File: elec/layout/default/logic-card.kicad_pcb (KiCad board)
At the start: 2 copper layers, 76 x 68 mm, 51 parts, among them U1 <help! no value>, U10 <help! no value>, U11 <help! no value>, U12 <help! no value>, U13 <help! no value>, U14 <help! no value>, U15 <help! no value>, U16 <help! no value>, U17 <help! no value>, U18 <help! no value>, U2 <help! no value>, U3 <help! no value>, U4 <help! no value>, U5 <help! no value>, U6 <help! no value>, U7 <help! no value>, U8 <help! no value>, U9 <help! no value>

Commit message: switch to coin cells
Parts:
- added U3: <help! no value>, lib:BAT-TH_BS-02-A1AJ010, B.Cu at (135.8, 120.6)
- added U4: <help! no value>, lib:BAT-TH_BS-02-A1AJ010, B.Cu at (161.3, 117.4)
- U2: footprint lib:BAT-TH_BH-AAA-A1AJ024 -> lib:BAT-TH_BS-02-A1AJ010
- moved U2 16.2 mm to (134.1, 92.8)
- renumbered U8 to U10, U9 to U11, U10 to U12, U11 to U13, U12 to U14, U13 to U15, U14 to U16, U15 to U17, U16 to U18, U17 to U19, U18 to U20, U3 to U5, U4 to U6, U5 to U7, U6 to U8, U7 to U9
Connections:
- C11 pad 1: vcc-2 -> vcc-3
- C12 pad 1: vcc-2 -> vcc-3
- C13 pad 1: vcc-2 -> vcc-3
- C14 pad 1: vcc-2 -> vcc-3
- U12 pad A4: vcc-3 -> vcc-4
- U12 pad A9: vcc-3 -> vcc-4
- U12 pad B4: vcc-3 -> vcc-4
- U12 pad B9: vcc-3 -> vcc-4
- U13 pad 2: vcc-3 -> vcc-4
- U2 pad 1: gnd -> gnd-1
- U2 pad 2: plus -> vcc-2
- U5 pad 1: plus -> vcc-2
- U7 pad 23: vcc-2 -> vcc-3
- U7 pad 45: vcc-2 -> vcc-3
- U7 pad 50: vcc-2 -> vcc-3
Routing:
- net plus: track 37.9 -> 0.00 mm
- net gnd-2: track 0.00 -> 35.1 mm
- net vcc-3: track 11.3 -> 33.3 mm, vias 0 -> 2
- net vcc-2: track 30.4 -> 44.5 mm, vias 2 -> 0
- net vcc-4: track 0.00 -> 11.3 mm
- net gnd-1: track 0.00 -> 8.49 mm
- net io3: track 14.3 -> 15.6 mm
- net gnd: vias 19 -> 21
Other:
- board text added: "San Francisco, December 2023"

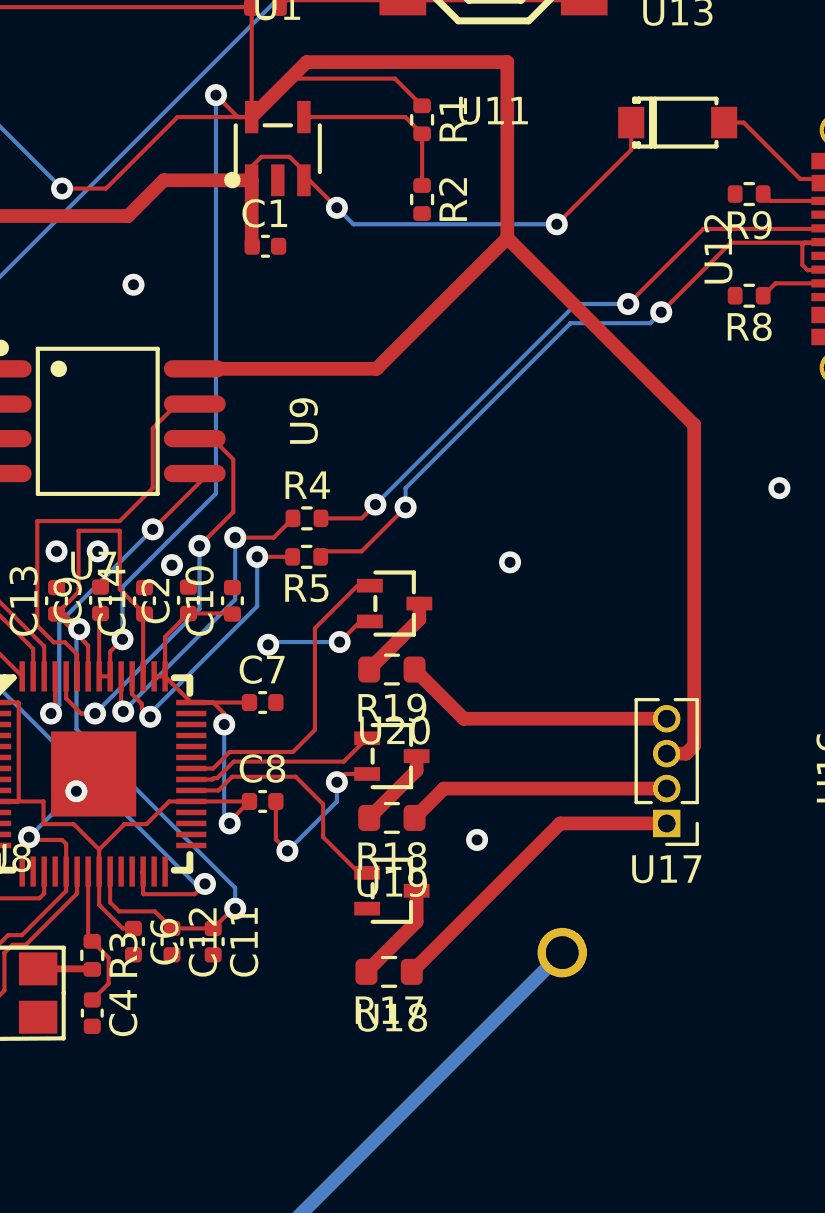
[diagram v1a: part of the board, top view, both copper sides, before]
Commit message: fix the led pins
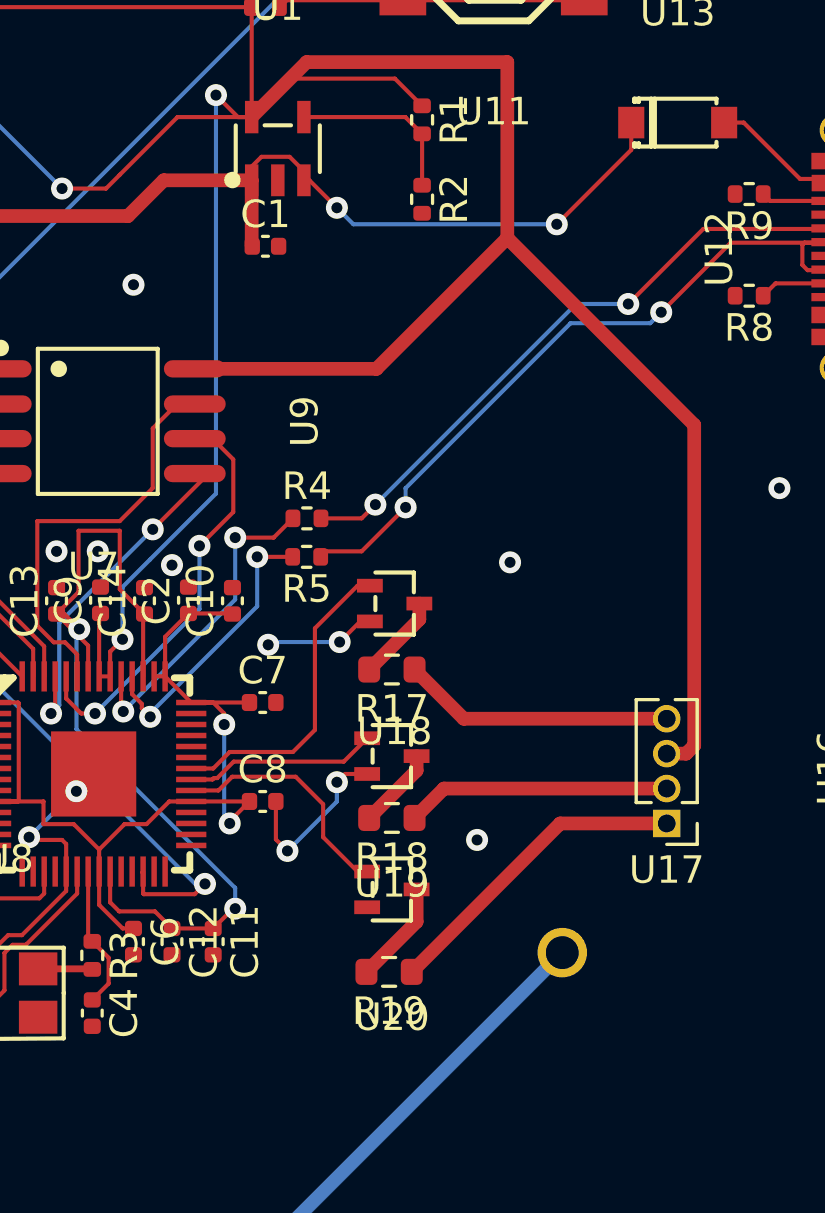
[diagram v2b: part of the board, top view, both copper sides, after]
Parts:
- C1, C10, C14, C2: value 1uF -> 1.0 uF
- C11, C12, C13, C5, C6, C7, C8, C9: value 100nF -> 100.0 nF
- C3, C4: value 20pF -> 22.0 pF
- R1: value 18k -> 18.0 KΩ
- R10, R11, R12, R13, R14, R15, R16, R2, R6, R7: value 10k -> 10.0 KΩ
- R17: value 1.5k -> 1.5 KΩ
- R18, R19: value 100 -> 100.0 Ω
- R3: value 1k -> 1.0 KΩ
- R4, R5: value 27R -> 27.0 Ω
- R8, R9: value 5.1k -> 4.7 KΩ
- U1, U10, U11, U12, U13, U14, U15, U16, U17, U18, U19, U2, U20, U3, U4, U5, U6, U7, U8, U9: value <help! no value> -> (none)
- moved R17 11.0 mm to (155.1, 97.1)
- moved R19 11.0 mm to (155.0, 108.1)
- moved U18 10.5 mm to (155.2, 94.7)
- moved U20 10.4 mm to (155.1, 105.1)
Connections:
- U17 pad 1: p1-1 -> p1-3
- U17 pad 4: p1-3 -> p1-1
- U18 pad 1: gpio22 -> gpio24
- U20 pad 1: gpio24 -> gpio22
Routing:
- net p1-3: track 9.92 -> 11.5 mm
- net p1-1: track 11.5 -> 9.92 mm
- net r_sink: track 3.71 -> 3.16 mm
- net b_sink: track 3.16 -> 3.71 mm

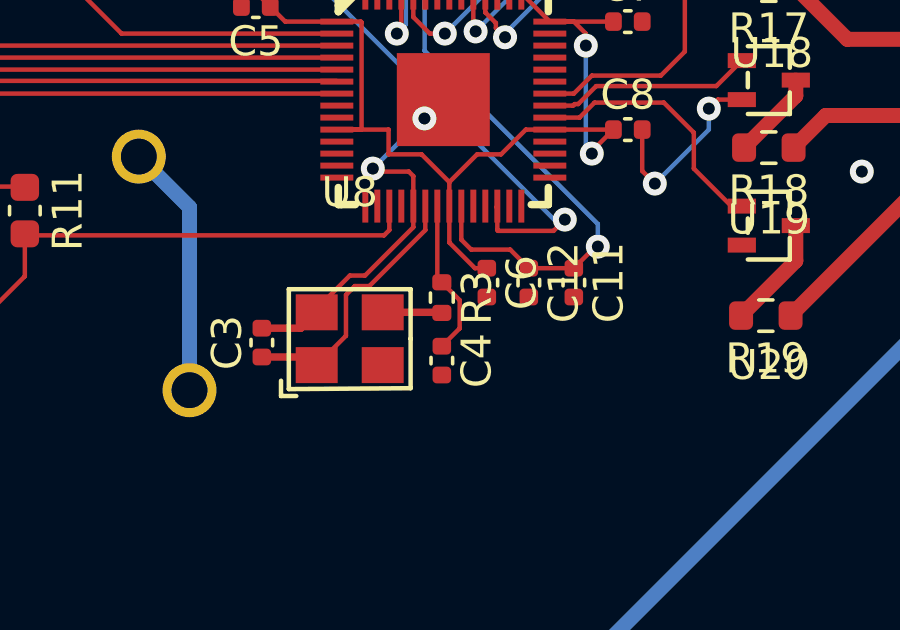
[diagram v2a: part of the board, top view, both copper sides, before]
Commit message: fix oscillator
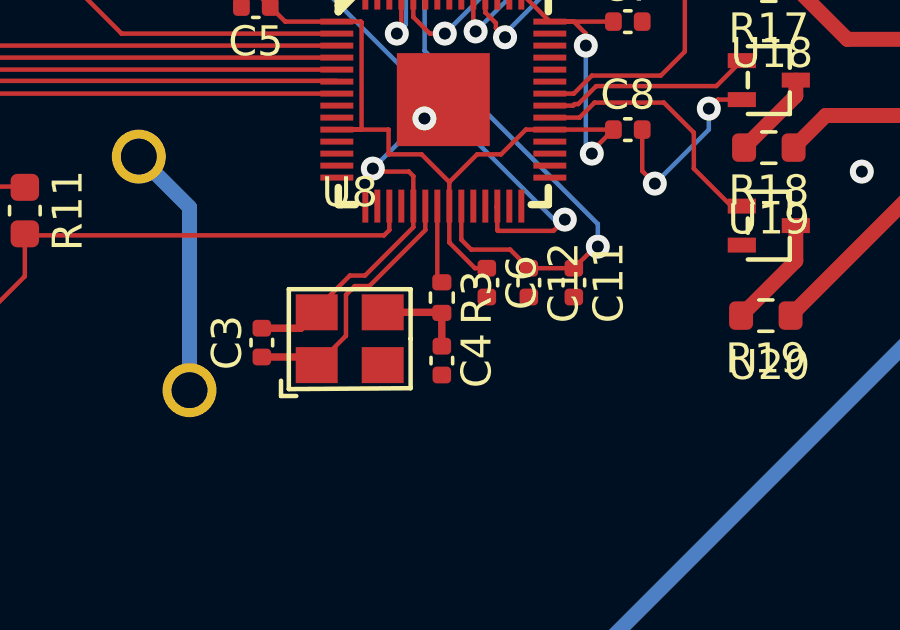
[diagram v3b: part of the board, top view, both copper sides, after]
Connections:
- C4 pad 1: p1 -> out-1
- R17 pad 1: p1-1 -> p1
- R18 pad 1: p1-2 -> p1-1
- R19 pad 1: p1-3 -> p1-2
- R3 pad 1: p1 -> xout
- U17 pad 1: p1-3 -> p1-2
- U17 pad 2: p1-2 -> p1-1
- U17 pad 4: p1-1 -> p1
- U7 pad 21: p1 -> xout
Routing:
- net p1-3: track 11.5 -> 0.00 mm
- net p1: track 5.23 -> 9.92 mm
- net xout: track 0.00 -> 2.60 mm
- net p1-2: track 9.62 -> 11.5 mm
- net out-1: track 1.98 -> 3.09 mm

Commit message: fix the build
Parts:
- C1, C10, C14, C2: value 1.0 uF -> Multilayer Ceramic Capacitors MLCC - SMD/SMT 1uF 6.3V 0402 RoHS
- C11, C12, C13, C5, C6, C7, C8, C9: value 100.0 nF -> Multilayer Ceramic Capacitors MLCC - SMD/SMT 100nF 10V 0402 RoHS
- C3, C4: value 22.0 pF -> Multilayer Ceramic Capacitors MLCC - SMD/SMT 20pF 50V 0402 RoHS
- R1: value 18.0 KΩ -> Chip Resistor - Surface Mount 18KOhms ±5% 1/16W 0402 RoHS
- R10, R11: value 10.0 KΩ -> Chip Resistor - Surface Mount 11KOhms ±5% 1/16W 0402 RoHS; footprint lib:C0603 -> lib:R0402
- R12, R13, R14, R15, R16, R2, R6, R7: value 10.0 KΩ -> Chip Resistor - Surface Mount 10KOhms ±5% 1/16W 0402 RoHS
- R17: value 1.5 KΩ -> Chip Resistor - Surface Mount 1.5KOhms ±5% 1/10W 0603 RoHS
- R18, R19: value 100.0 Ω -> Chip Resistor - Surface Mount 100Ohms ±5% 1/10W 0603 RoHS
- R3: value 1.0 KΩ -> Chip Resistor - Surface Mount 1KOhms ±5% 1/16W 0402 RoHS
- R4, R5: value 27.0 Ω -> Chip Resistor - Surface Mount 27KOhms ±5% 1/16W 0402 RoHS
- R8, R9: value 4.7 KΩ -> Chip Resistor - Surface Mount 4.7KOhms ±5% 1/16W 0402 RoHS
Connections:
- net adj renamed io
- C3 pad 1: xin -> vcc-4
- C4 pad 1: out-1 -> vcc-5
- R3 pad 2: out-1 -> vcc-5
- U12 pad A4: vcc-4 -> vcc-6
- U12 pad A9: vcc-4 -> vcc-6
- U12 pad B4: vcc-4 -> vcc-6
- U12 pad B9: vcc-4 -> vcc-6
- U13 pad 2: vcc-4 -> vcc-6
- U16 pad 8: out-2 -> out-1
- U7 pad 20: xin -> vcc-4
- U8 pad 1: xin -> vcc-4
- U8 pad 3: out-1 -> vcc-5
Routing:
- net vcc-6: track 0.00 -> 11.3 mm
- net xin: track 9.03 -> 0.00 mm
- net vcc-5: track 0.00 -> 3.09 mm
- net out-1: track 3.09 -> 0.00 mm
- net vcc-4: track 11.3 -> 9.03 mm
